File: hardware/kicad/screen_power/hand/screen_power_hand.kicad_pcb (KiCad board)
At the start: 4 copper layers, 130 x 120 mm, 56 parts, among them J1 AUX 5V INPUT, J101 PI USB, J102 TOUCH, J103 EVM 5V, J104 EVM CONTROL, J2 SCREEN CONTROL, J201 PI USB, J202 TOUCH, J203 EVM 5V, J204 EVM CONTROL, K101 G6K-2P-RF DC5, K102 G5LE-1 DC5, K201 G6K-2P-RF DC5, K202 G5LE-1 DC5, Q1 2N3904, Q101 2N7000, Q102 2N3906, Q103 IRLZ44NPBF, Q104 2N7000, Q201 2N7000, Q202 2N3906, Q203 IRLZ44NPBF, Q204 2N7000

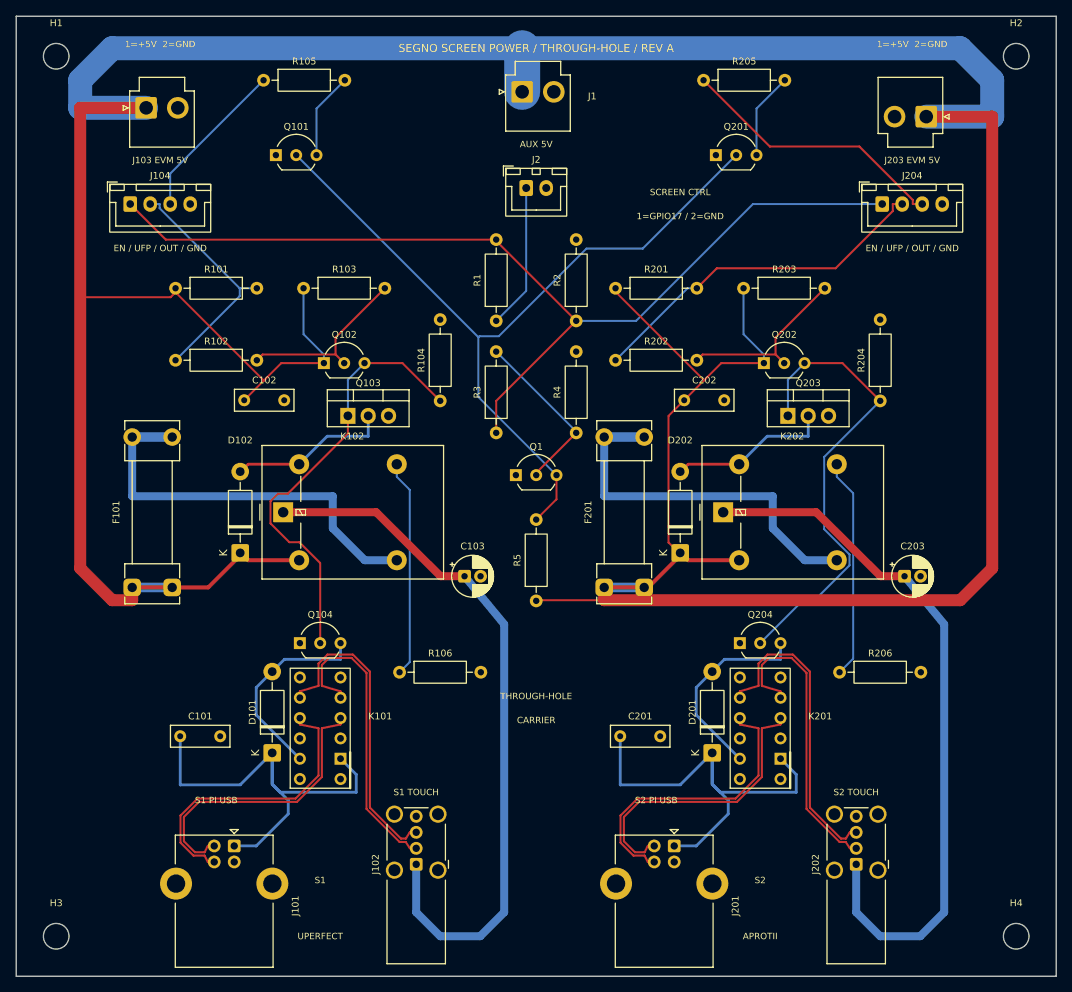
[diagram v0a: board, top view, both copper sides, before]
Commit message: refactor(hardware): simplify and compact screen power boards
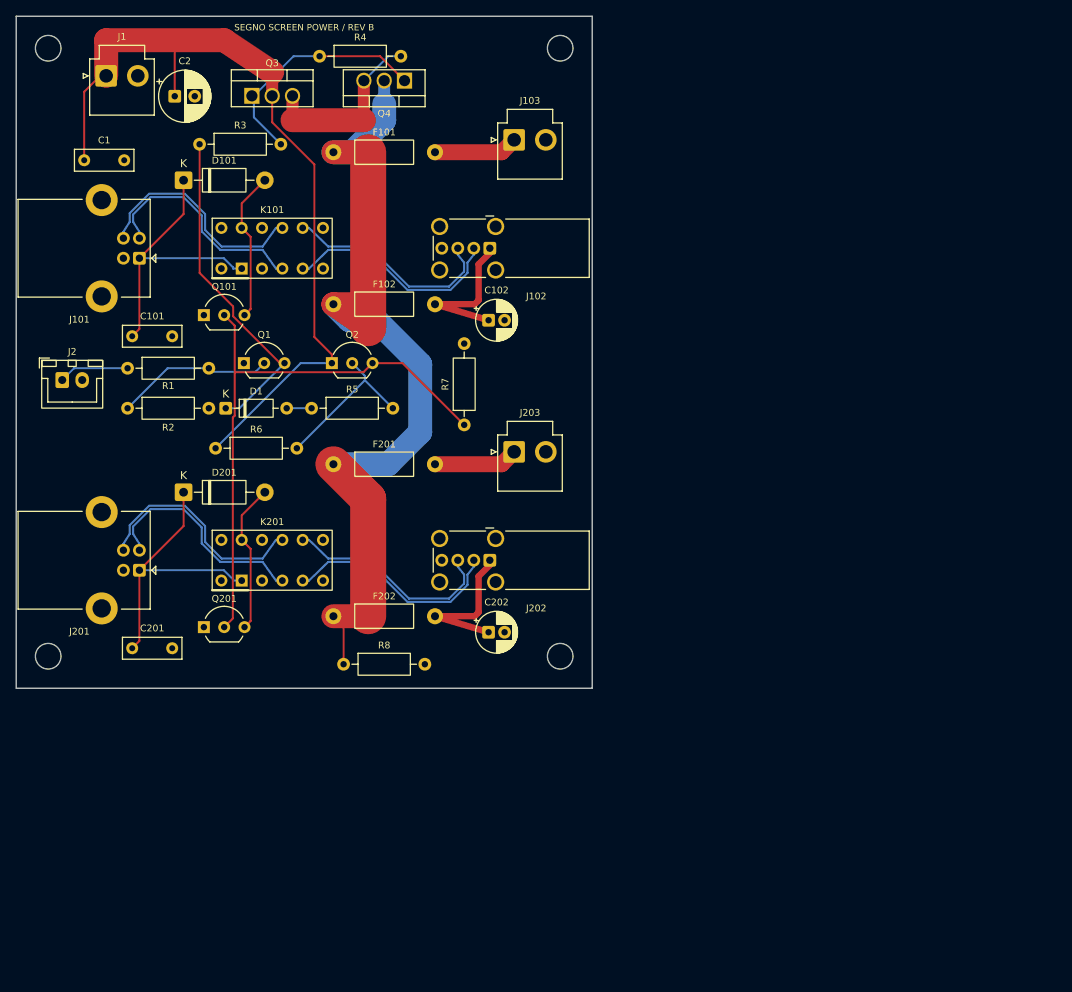
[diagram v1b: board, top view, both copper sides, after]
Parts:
- removed C103, C203: 150uF 10V, CP_Radial_D5.0mm_P2.00mm
- removed D102, D202: 1N4007, D_DO-41_SOD81_P10.16mm_Horizontal
- removed J104, J204: EVM CONTROL, JST_XH_B4B-XH-A_1x04_P2.50mm_Vertical
- removed K102, K202: G5LE-1 DC5, Relay_SPDT_Omron-G5LE-1
- removed Q102, Q202: 2N3906, TO-92_Inline_Wide
- removed Q103, Q203: IRLZ44NPBF, TO-220-3_Vertical
- removed Q104, Q204: 2N7000, TO-92_Inline_Wide
- removed R101, R103, R104, R201, R203, R204: 100k 1%, R_Axial_DIN0207_L6.3mm_D2.5mm_P10.16mm_Horizontal
- removed R102, R202: 5.6k 1%, R_Axial_DIN0207_L6.3mm_D2.5mm_P10.16mm_Horizontal
- removed R105, R106, R205, R206: 100R 1W 1%, R_Axial_DIN0207_L6.3mm_D2.5mm_P10.16mm_Horizontal
- added C1: 100nF 63V, C_Rect_L7.2mm_W2.5mm_P5.00mm, F.Cu at (8.50, 18.0)
- added C2: 220uF 10V, CP_Radial_D6.3mm_P2.50mm, F.Cu at (19.8, 10.0)
- added D1: 1N4148, D_DO-35_SOD27_P7.62mm_Horizontal, F.Cu at (26.2, 49.0)
- added F102: 750mA fast, Fuse_Littelfuse_251_P12.70mm, F.Cu at (39.6, 36.0)
- added F202: 750mA fast, Fuse_Littelfuse_251_P12.70mm, F.Cu at (39.6, 75.0)
- added Q2: 2N3906, TO-92_Inline_Wide, F.Cu at (39.5, 43.4)
- added Q3: SUP70101EL, TO-220-3_SUP70101EL, F.Cu at (29.5, 9.95)
- added Q4: SUP70101EL, TO-220-3_SUP70101EL, F.Cu at (48.5, 8.05)
- added R6: 100k 1%, R_Axial_DIN0207_L6.3mm_D2.5mm_P10.16mm_Horizontal, F.Cu at (24.9, 54.0)
- added R7: 100k 1%, R_Axial_DIN0207_L6.3mm_D2.5mm_P10.16mm_Horizontal, F.Cu at (56.0, 51.1)
- added R8: 100R 1W 1%, R_Axial_DIN0207_L6.3mm_D2.5mm_P10.16mm_Horizontal, F.Cu at (40.9, 81.0)
- C102, C202: value 100nF 63V -> 150uF 10V; footprint C_Rect_L7.2mm_W2.5mm_P5.00mm -> CP_Radial_D5.0mm_P2.00mm
- F101, F201: value 0.8A fast / two clips -> 4A fast; footprint Fuseholder_Clip-5x20mm_Littelfuse_111_Lateral_P18.80x5.00mm_D1.17mm_Horizontal -> Fuse_Littelfuse_251_P12.70mm
- J103: value EVM 5V -> SCREEN 1 POWER
- J2: value SCREEN CONTROL -> GPIO17 / GND
- J203: value EVM 5V -> SCREEN 2 POWER
- R2: value 10k 1% -> 100k 1%
- R3: value 10k 1% -> 4.7k 1%
- R4: value 100k 1% -> 330k 1%
- R5: value 10k 1% -> 5.6k 1%
- moved Q201 87.0 mm to (23.5, 76.4)
- moved J102 77.6 mm to (59.2, 29.0), turned to 180 degrees
- moved J201 75.2 mm to (15.4, 69.2), turned to 180 degrees
- moved J101 74.4 mm to (15.4, 30.2), turned to 180 degrees
- moved D201 73.7 mm to (20.9, 59.5), turned to 0 degrees
- moved D101 72.4 mm to (20.9, 20.5), turned to 0 degrees
- moved H4 66.9 mm to (68.0, 80.0)
- moved J203 66.4 mm to (62.2, 54.5), turned to 0 degrees
- moved K201 64.5 mm to (32.0, 68.0), turned to 0 degrees
- moved J2 62.8 mm to (5.75, 45.5)
- moved C201 62.0 mm to (14.5, 79.0)
- moved K101 60.3 mm to (32.0, 29.0), turned to 0 degrees
- moved F101 59.9 mm to (39.6, 17.0), turned to 0 degrees
- moved J202 59.5 mm to (59.2, 68.0), turned to 180 degrees
- moved R2 57.1 mm to (13.9, 49.0), turned to 0 degrees
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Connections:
- C102 pad 1: AUX_5V -> S1_TOUCH_5V
- C202 pad 1: AUX_5V -> S2_TOUCH_5V
- F101 pad 1: AUX_5V -> SWITCHED_5V
- F101 pad 2: S1_TOUCH_FUSED -> S1_MAIN_5V
- F201 pad 1: AUX_5V -> SWITCHED_5V
- F201 pad 2: S2_TOUCH_FUSED -> S2_MAIN_5V
- J103 pad 1: AUX_5V -> S1_MAIN_5V
- J203 pad 1: AUX_5V -> S2_MAIN_5V
- Q1 pad 2: DUMP_BASE -> CONTROL_BASE
- Q1 pad 3: DISCHARGE -> CONTROL_SINK
- Q101 pad 2: DISCHARGE -> DATA_ENABLE
- Q101 pad 3: S1_MAIN_DUMP -> S1_DATA_COIL_LOW
- Q201 pad 2: DISCHARGE -> DATA_ENABLE
- Q201 pad 3: S2_MAIN_DUMP -> S2_DATA_COIL_LOW
- R1 pad 2: DISPLAY_ENABLE -> CONTROL_BASE
- R2 pad 1: DISPLAY_ENABLE -> CONTROL_BASE
- R3 pad 1: DISPLAY_ENABLE -> CONTROL_SINK
- R3 pad 2: DUMP_BASE -> POWER_GATE
- R4 pad 1: DUMP_BASE -> POWER_GATE
- R4 pad 2: GND -> COMMON_SOURCE
- R5 pad 1: AUX_5V -> BUFFER_SINK
- R5 pad 2: DISCHARGE -> BUFFER_BASE
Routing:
- net AUX_5V: track 509.8 -> 103.5 mm
- net DISPLAY_ENABLE: track 124.3 -> 0.00 mm
- net SWITCHED_5V: track 0.00 -> 115.4 mm
- net DISCHARGE: track 101.8 -> 0.00 mm
- net DATA_ENABLE: track 0.00 -> 72.4 mm
- net S2_TOUCH_5V: track 89.2 -> 19.7 mm
- net S1_TOUCH_5V: track 89.2 -> 19.7 mm
- net S2_TOUCH_EN: track 58.8 -> 0.00 mm
- net S1_TOUCH_EN: track 55.3 -> 0.00 mm
- net S1_TOUCH_FUSED: track 51.1 -> 0.00 mm
- net S2_TOUCH_FUSED: track 47.1 -> 0.00 mm
- net S2_UFP_N: track 44.4 -> 0.00 mm
- net CONTROL_SINK: track 0.00 -> 41.8 mm
- net S1_UFP_N: track 30.3 -> 0.00 mm
- net POWER_GATE: track 0.00 -> 29.8 mm
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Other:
- board size 130 x 120 mm -> 72 x 84 mm
- board text added: "1=5V 2=GND"
- board text added: "4L / GND L2 L3"
- board text added: "5V IN"
- board text added: "GPIO17 / GND"
- board text added: "S1 5V OUT"
- board text added: "S1 PI"
- board text added: "S2 5V OUT"
- board text added: "S2 PI"
- board text added: "SEGNO SCREEN POWER / REV B"
- board text added: "USB 90 OHM"
- board text removed: "1=+5V 2=GND"
- board text removed: "1=GPIO17 / 2=GND"
- board text removed: "4L / 1.6mm"
- board text removed: "APROTII"
- board text removed: "AUX 5V"
- board text removed: "CARRIER"
- board text removed: "CONFIRM 90 OHM"
- board text removed: "EN / UFP / OUT / GND"
- board text removed: "GND: INNER 1+2"
- board text removed: "J103 EVM 5V"
- board text removed: "J203 EVM 5V"
- board text removed: "JLC04161H-7628"
- board text removed: "S1"
- board text removed: "S1 PI USB"
- board text removed: "S2"
- board text removed: "S2 PI USB"
- board text removed: "SCREEN CTRL"
- board text removed: "SEGNO SCREEN POWER / THROUGH-HOLE / REV A"
- board text removed: "THROUGH-HOLE"
- board text removed: "UPERFECT"
- board text removed: "USB: 0.26/0.16mm"

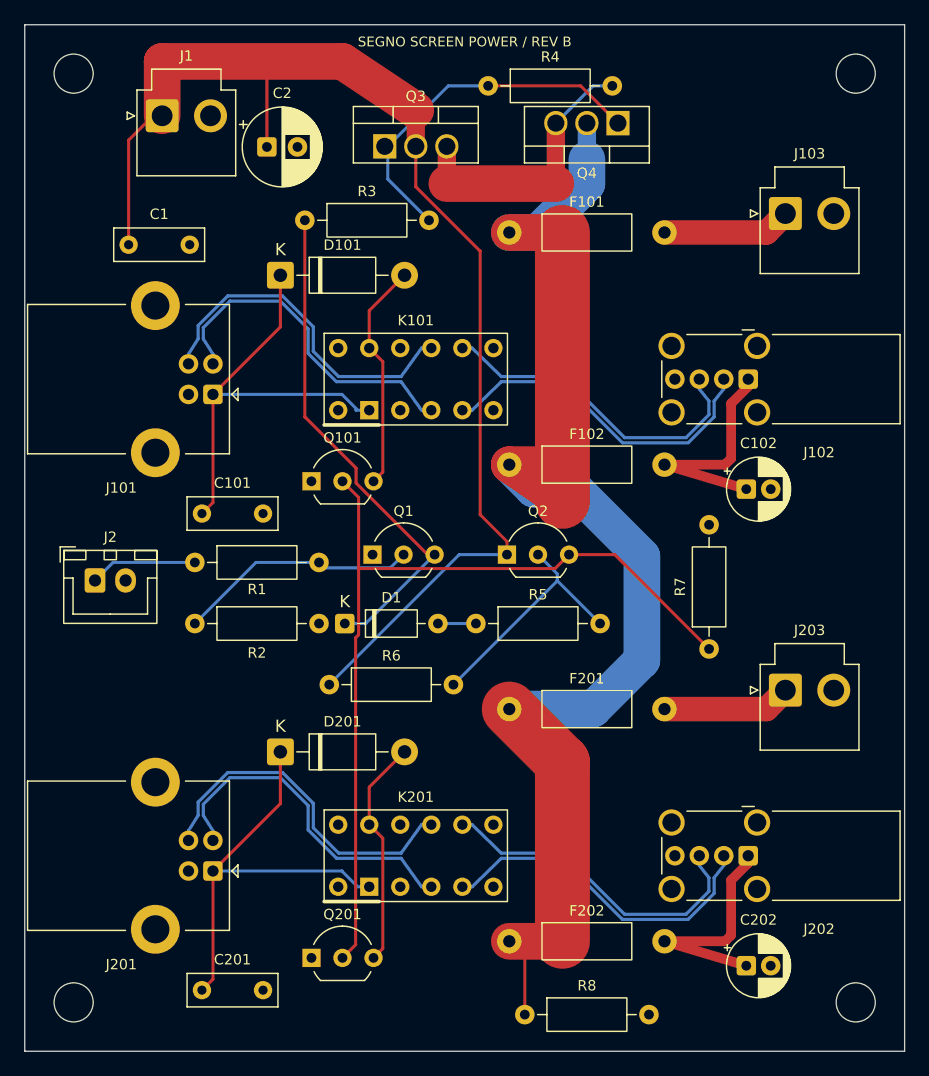
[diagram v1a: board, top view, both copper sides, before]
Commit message: feat(hardware): publish screen switching and board refinements
Add the hand-soldered two-layer screen-power board, aligned console connectors, ADC supply isolation, white ring carrier and reviewed manufacturing ZIPs. Integrate GPIO17 ownership with Weston startup and shutdown; retain assembled-system validation as the hardware gate.
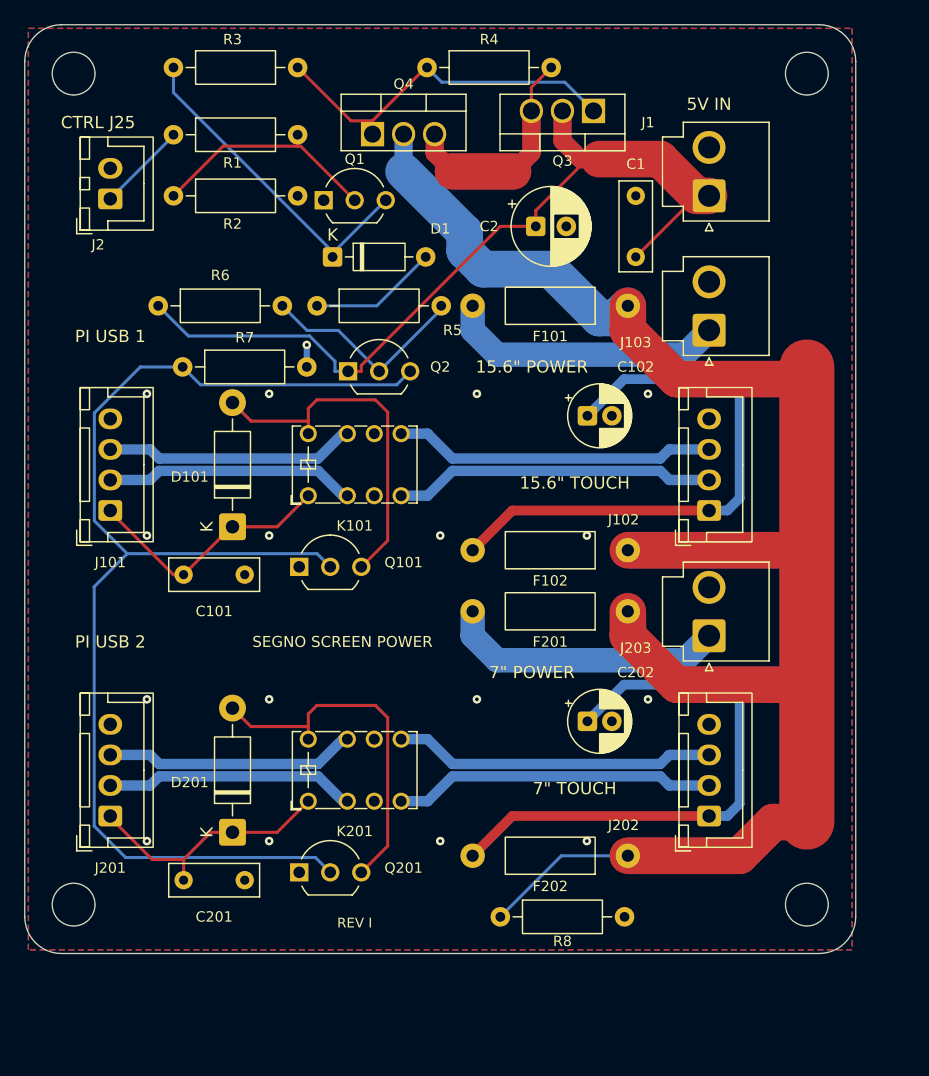
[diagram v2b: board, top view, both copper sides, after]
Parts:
- H1, H2, H3, H4: footprint MountingHole_3.2mm_M3 -> MountingHole_3.5mm
- J101, J201: value PI USB -> PI USB / XH4; footprint USB_B_Lumberg_2411_06_Horizontal -> JST_XH_B4B-XH-A_1x04_P2.50mm_Vertical
- J102, J202: value TOUCH -> TOUCH / XH4; footprint USB_A_Wuerth_614004134726_Horizontal -> JST_XH_B4B-XH-A_1x04_P2.50mm_Vertical
- K101, K201: value G6K-2P-RF DC5 -> IM02TS; footprint Relay_DPDT_Omron_G6K-2P-RF -> Relay_DPDT_AXICOM_IMSeries_Pitch5.08mm_D0.90mm
- moved R7 48.9 mm to (12.9, 28.0), turned to 0 degrees
- moved J1 45.2 mm to (56.0, 14.0), turned to 90 degrees
- moved C1 41.5 mm to (50.0, 19.0), turned to 90 degrees
- moved R1 35.0 mm to (12.2, 9.00)
- moved R2 35.0 mm to (12.2, 14.0)
- moved R6 34.0 mm to (10.9, 23.0)
- moved J2 31.3 mm to (7.00, 14.2), turned to 90 degrees
- moved D1 30.0 mm to (25.2, 19.0)
- moved Q1 29.3 mm to (24.5, 14.4)
- moved R5 29.1 mm to (23.9, 23.0)
- moved C202 23.9 mm to (46.0, 57.0)
- moved C2 22.9 mm to (41.8, 16.5)
- moved D101 21.0 mm to (17.0, 41.1), turned to 90 degrees
- moved Q4 20.1 mm to (28.5, 8.95), turned to 0 degrees
- moved Q2 19.8 mm to (26.5, 28.4)
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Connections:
- K101 pad 2: (no net) -> S1_UP_N
- K101 pad 3: S1_UP_N -> (no net)
- K101 pad 6: S1_UP_P -> (no net)
- K101 pad 7: (no net) -> S1_UP_P
- K201 pad 2: (no net) -> S2_UP_N
- K201 pad 3: S2_UP_N -> (no net)
- K201 pad 6: S2_UP_P -> (no net)
- K201 pad 7: (no net) -> S2_UP_P
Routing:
- net AUX_5V: track 103.5 -> 68.1 mm
- net DATA_ENABLE: track 72.4 -> 102.5 mm
- net SWITCHED_5V: track 115.4 -> 144.5 mm
- net S2_TOUCH_5V: track 19.7 -> 46.5 mm
- net S1_TOUCH_5V: track 19.7 -> 46.5 mm
- net CONTROL_SINK: track 41.8 -> 27.0 mm
- net HOST1_5V: track 35.6 -> 21.1 mm
- net HOST2_5V: track 35.6 -> 21.4 mm
- net S2_MAIN_5V: track 10.5 -> 23.0 mm
- net S1_MAIN_5V: track 10.5 -> 23.0 mm
- net S2_DATA_COIL_LOW: track 18.8 -> 29.6 mm
- net S1_DATA_COIL_LOW: track 18.8 -> 29.6 mm
- net S1_UP_P: track 28.6 -> 20.6 mm
- net S2_UP_P: track 28.6 -> 20.6 mm
- net BUFFER_SINK: track 3.11 -> 10.5 mm
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- added copper zone on B.Cu, net GND
- added copper zone on F.Cu, net GND
- removed copper zone on In1.Cu, net GND
- removed copper zone on In2.Cu, net GND
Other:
- board size 72 x 84 mm -> 68 x 76 mm
- copper layers 4 -> 2
- board text added: "1 +5V"
- board text added: "15.6" POWER"
- board text added: "15.6" TOUCH"
- board text added: "2 D-"
- board text added: "2 LAYERS"
- board text added: "3 D+"
- board text added: "4 GND"
- board text added: "7" POWER"
- board text added: "7" TOUCH"
- board text added: "CTRL J25"
- board text added: "PI USB 1"
- board text added: "PI USB 2"
- board text added: "REV I"
- board text added: "SEGNO SCREEN POWER"
- board text added: "SEGNO SCREEN POWER / REV I"
- board text removed: "4L / GND L2 L3"
- board text removed: "SEGNO SCREEN POWER / REV B"
- board text removed: "USB 90 OHM"

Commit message: fix(hardware): correct screen relay contacts and strengthen power routing
Replace withdrawn Revision I with checked Revision J fabrication files. Correct USB relay commons, reinforce the shared power paths, and verify relay states and a fuse-barrel-independent via path. Record the requested Claude review and independent follow-up checks.
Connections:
- K101 pad 2: S1_UP_N -> (no net)
- K101 pad 3: (no net) -> S1_UP_N
- K101 pad 6: (no net) -> S1_UP_P
- K101 pad 7: S1_UP_P -> (no net)
- K201 pad 2: S2_UP_N -> (no net)
- K201 pad 3: (no net) -> S2_UP_N
- K201 pad 6: (no net) -> S2_UP_P
- K201 pad 7: S2_UP_P -> (no net)
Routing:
- net SWITCHED_5V: track 144.5 -> 149.6 mm, vias 0 -> 3
- net S2_UP_P: track 20.6 -> 23.4 mm
- net S2_UP_N: track 20.6 -> 23.4 mm
- net S1_UP_N: track 20.6 -> 23.4 mm
- net S1_UP_P: track 20.6 -> 23.4 mm
- net AUX_5V: track 68.1 -> 69.5 mm
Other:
- board text added: "REV J"
- board text added: "SEGNO SCREEN POWER / REV J"
- board text removed: "2 LAYERS"
- board text removed: "REV I"
- board text removed: "SEGNO SCREEN POWER / REV I"
